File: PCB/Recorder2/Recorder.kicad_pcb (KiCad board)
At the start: 2 copper layers, 70 x 70 mm, 57 parts, among them J1 Reset, J2 JST-PH-SM4-TB, J3 TC2030-USB-NL-DS, J4 TF_PUSH, J5 USB-C-Socket-H, Q1 CJ2301, SW1 SW_Push_DPDT, U1 ESP32-S3-MINI-1-N4R2, U3 TP4054, U4 ME6211C33M5G-N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

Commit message: Tracked for order
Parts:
- moved R1 11.9 mm to (109.2, 108.4), turned to -90 degrees
- moved R14 11.5 mm to (93.0, 109.3), turned to 90 degrees
- moved R15 10.7 mm to (92.0, 109.3), turned to -90 degrees
- moved R16 9.90 mm to (91.0, 109.3), turned to 90 degrees
- moved J1 2.30 mm to (120.2, 105.7)
- moved C2 1.98 mm to (108.4, 92.7)
- moved R8 1.52 mm to (111.6, 92.9), turned to 0 degrees
- moved C15 1.50 mm to (89.0, 92.0)
- moved R2 1.32 mm to (109.0, 92.1)
- moved D9 1.00 mm to (90.5, 92.0)
- moved C14 0.70 mm to (106.2, 110.3)
- moved C13 0.42 mm to (89.0, 107.0)
- turned J3 to 0 degrees
- turned R12 to 180 degrees
- turned R13 to 0 degrees
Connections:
- net VIN renamed Net-(D3-K)
- R1 pad 1: Net-(U1-GPIO41) -> Net-(U1-GPIO48)
- U1 pad 12: LEDMIC -> unconnected-(U1-GPIO8-Pad12)
- U1 pad 13: unconnected-(U1-GPIO9-Pad13) -> LEDMIC
- U1 pad 14: unconnected-(U1-GPIO10-Pad14) -> ADC
- U1 pad 15: CHARGING -> ADCL
- U1 pad 29: unconnected-(U1-GPIO34-Pad29) -> BLINK
- U1 pad 30: unconnected-(U1-GPIO48-Pad30) -> Net-(U1-GPIO48)
- U1 pad 35: BLINK -> unconnected-(U1-GPIO39-Pad35)
- U1 pad 37: Net-(U1-GPIO41) -> unconnected-(U1-GPIO41-Pad37)
- U1 pad 5: BTN -> CHARGING
- U1 pad 7: unconnected-(U1-GPIO3-Pad7) -> BTN
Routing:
- net +3V3: track 0.00 -> 113.6 mm, vias 0 -> 7
- net GND: track 0.00 -> 75.2 mm, vias 0 -> 30
- net VSWITCHED: track 0.00 -> 61.8 mm, vias 0 -> 3
- net D-: track 0.00 -> 55.7 mm, vias 0 -> 2
- net D+: track 0.00 -> 55.1 mm, vias 0 -> 2
- net VBUS: track 0.00 -> 33.3 mm, vias 0 -> 2
- net SCK: track 0.00 -> 32.5 mm, vias 0 -> 3
- net WS: track 0.00 -> 31.0 mm, vias 0 -> 4
- net PWR: track 0.00 -> 28.9 mm, vias 0 -> 2
- net VBAT: track 0.00 -> 25.9 mm, vias 0 -> 2
- net SD: track 0.00 -> 25.6 mm, vias 0 -> 1
- net BTN: track 0.00 -> 23.6 mm, vias 0 -> 2
- net Net-(J1-Pin_2): track 0.00 -> 23.1 mm, vias 0 -> 3
- net CHARGING: track 0.00 -> 18.4 mm, vias 0 -> 2
- net Net-(D7-O): track 0.00 -> 18.1 mm, vias 0 -> 2
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- added copper zone on F.Cu, net VBUS
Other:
- board text added: "${CURRENT_DATE}"
- board text added: "1 2 3 5 6 7 9 10 11"
- board text added: "12 13 14 15 16 17 18"
- board text added: "34 48"
- board text added: "A"
- board text added: "Baking not required X-ray not required"
- board text added: "CHG PWR BTN SCK WS SD LEDMIC ADC ADCL"
- board text added: "DAT2 DAT3 CMD CLK DAT0 DAT1 CD"
- board text added: "L"
- board text added: "LEDS VBUS"
- board text added: "Made in China for Andrews&Arnold Ltd"
- board text added: "OpenMic"
- board text added: "R"
- board text added: "openmic.revk.uk"
- board text removed: "Baking not required"

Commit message: Re render
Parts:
- C10, C11: footprint RevK:C_0402 -> RevK:C_0201
- R11, R14, R15, R16: footprint RevK:R_0402 -> RevK:R_0201
- R8: value 10K -> 5K1; footprint RevK:R_0402 -> RevK:R_0201
- U5: value L -> ICS-43434
- U6: value R -> ICS-43434
- moved U5 21.0 mm to (87.0, 89.0), turned to 90 degrees
- moved U6 21.0 mm to (87.0, 110.0), turned to -90 degrees
- moved D1 0.80 mm to (118.2, 100.0)
- moved J5 0.50 mm to (119.5, 92.5)
- moved D2 0.40 mm to (120.1, 100.5)
- moved R14 0.32 mm to (92.7, 109.2), turned to -90 degrees
- moved R16 0.32 mm to (91.3, 109.2), turned to -90 degrees
- moved J4 0.10 mm to (94.7, 100.5)
- moved R15 0.10 mm to (92.0, 109.2), turned to 90 degrees
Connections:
- R16 pad 2: ADCL -> GND
- U1 pad 14: ADC -> unconnected-(U1-GPIO10-Pad14)
- U1 pad 15: ADCL -> ADC
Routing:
- net ADC: track 12.4 -> 4.28 mm, vias 2 -> 0
- net ADCL: track 3.91 -> 0.00 mm
- net +3V3: track 113.6 -> 109.9 mm
- net VBAT: track 25.9 -> 28.2 mm
- net GND: track 75.2 -> 74.2 mm, vias 30 -> 33
- net VSWITCHED: track 61.8 -> 62.7 mm
- net PWR: track 28.9 -> 28.2 mm
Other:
- board text added: "1 2 3 5 6 7 9 11"
- board text added: "Audio Recorder"
- board text added: "CHG PWR BTN SCK WS SD LEDMIC ADC"
- board text removed: "1 2 3 5 6 7 9 10 11"
- board text removed: "CHG PWR BTN SCK WS SD LEDMIC ADC ADCL"

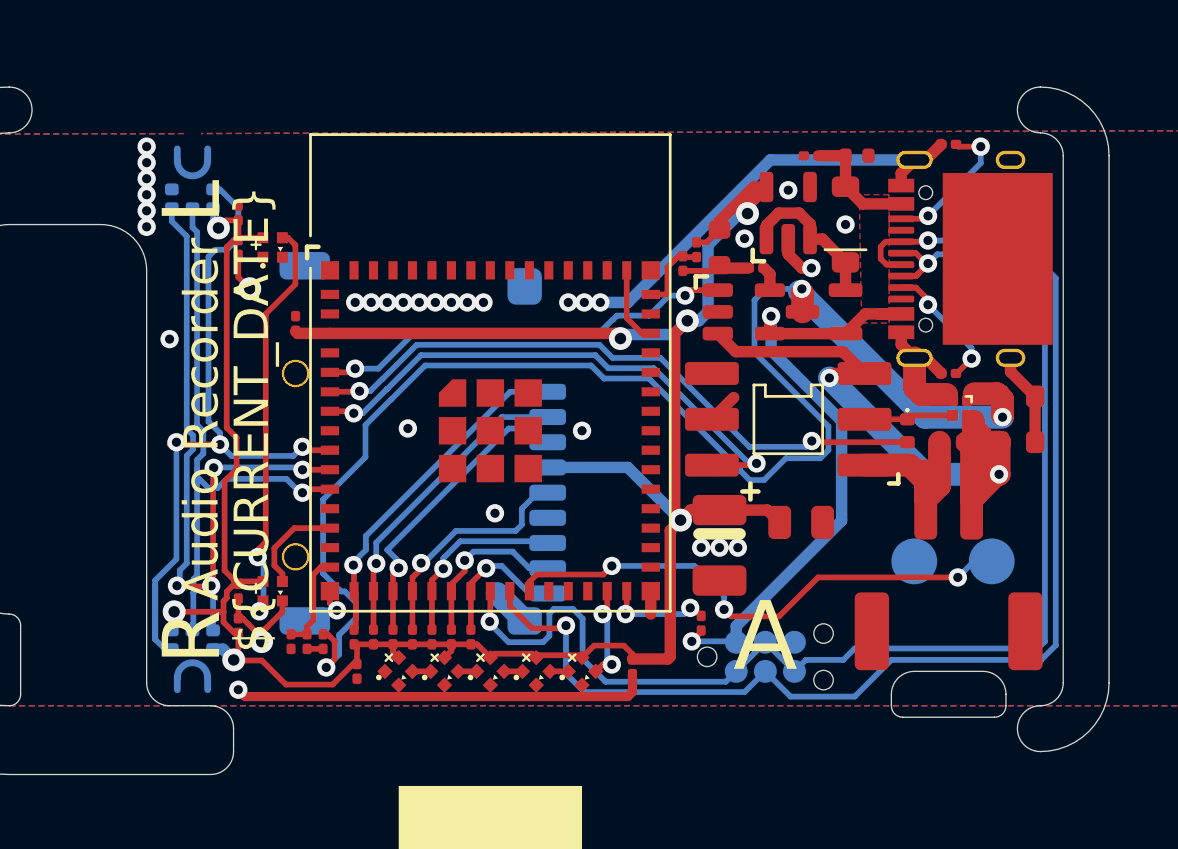
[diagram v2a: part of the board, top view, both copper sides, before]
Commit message: Layout tweaks
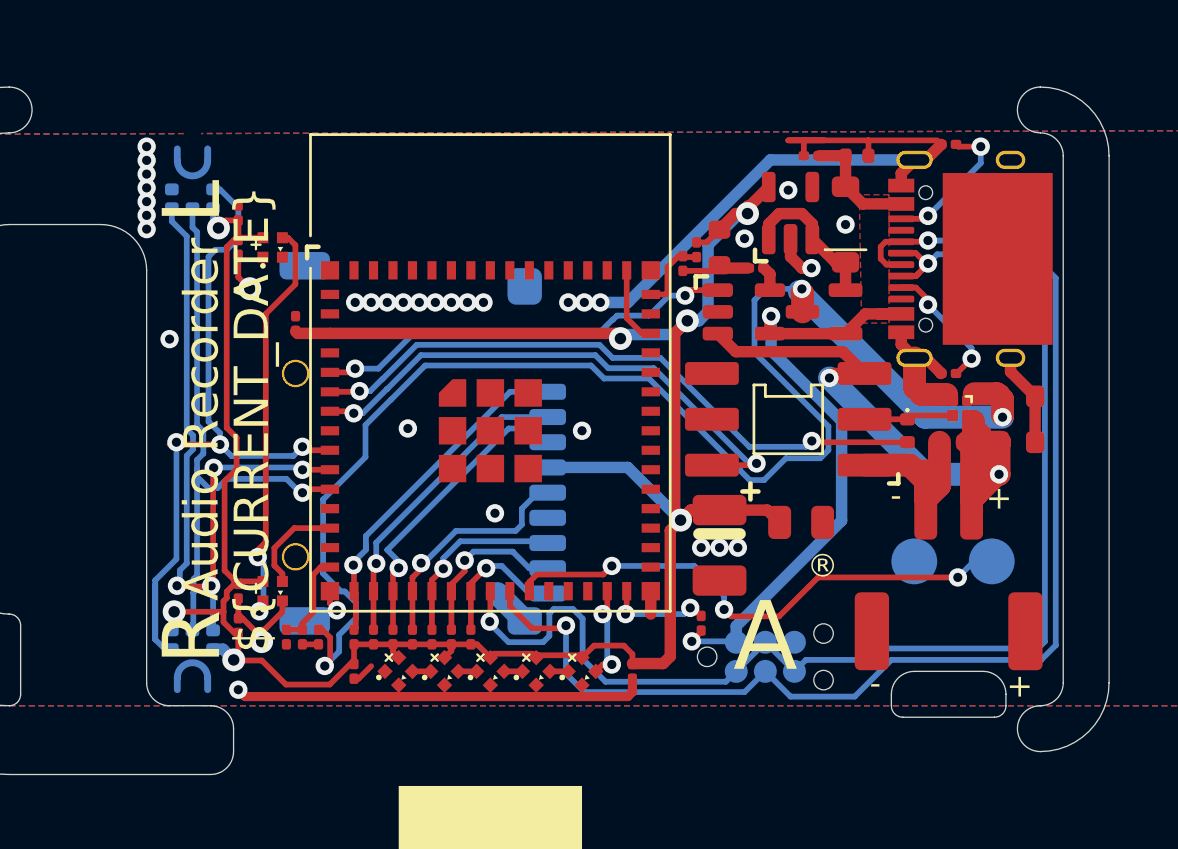
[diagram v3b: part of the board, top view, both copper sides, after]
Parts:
- U2: value ~ -> TPS22916CNYFPR
- moved R14 0.28 mm to (92.5, 109.0)
- moved R15 0.28 mm to (91.8, 109.0)
- moved R16 0.28 mm to (91.1, 109.0)
- moved C14 0.20 mm to (106.2, 110.5)
- moved C12 0.13 mm to (94.0, 110.5)
- moved U4 0.10 mm to (113.1, 90.5)
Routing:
- net GND: track 74.2 -> 83.0 mm, vias 33 -> 34
- net +3V3: track 109.9 -> 108.7 mm
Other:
- board text added: "+"
- board text added: "-"
- board text added: "21"
- board text added: "®"

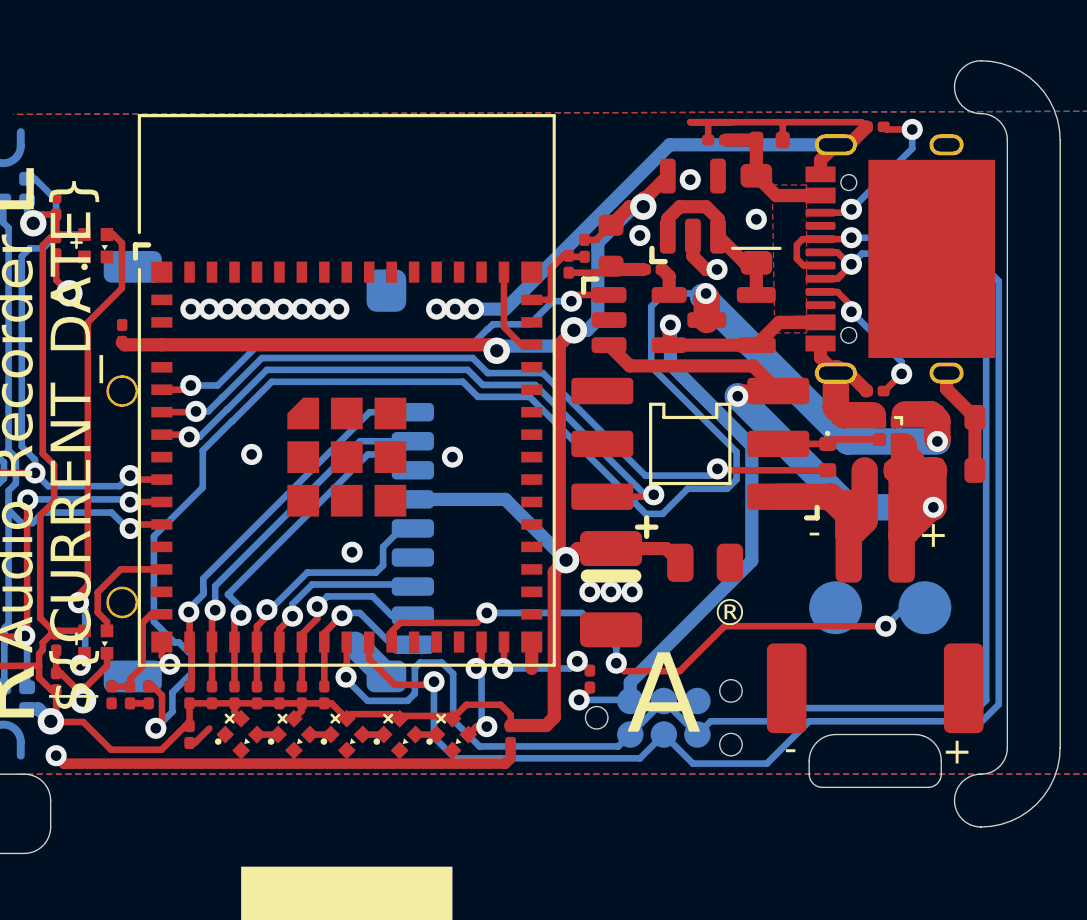
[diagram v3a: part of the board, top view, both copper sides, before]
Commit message: Moved GPIOs around a bit
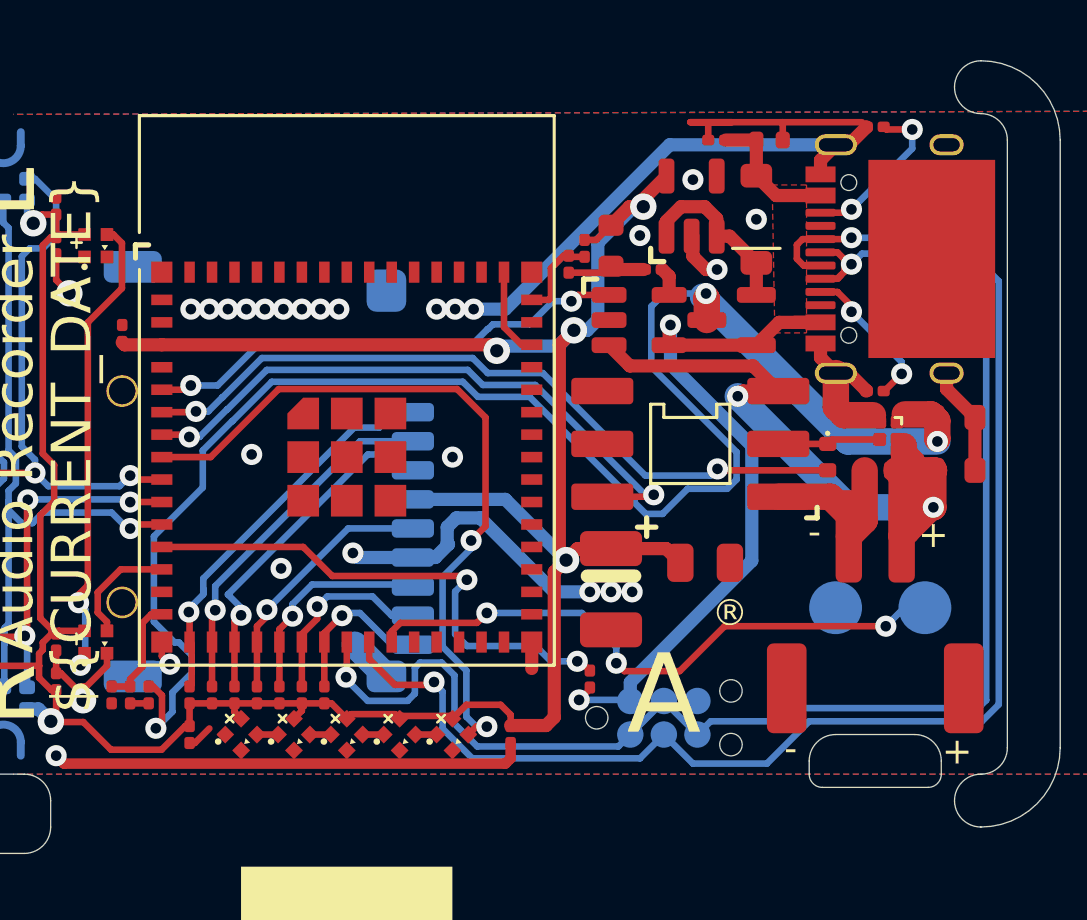
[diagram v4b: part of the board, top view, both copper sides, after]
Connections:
- R1 pad 1: Net-(U1-GPIO48) -> Net-(U1-GPIO8)
- U1 pad 12: unconnected-(U1-GPIO8-Pad12) -> Net-(U1-GPIO8)
- U1 pad 29: BLINK -> unconnected-(U1-GPIO34-Pad29)
- U1 pad 30: Net-(U1-GPIO48) -> unconnected-(U1-GPIO48-Pad30)
- U1 pad 8: unconnected-(U1-GPIO4-Pad8) -> BLINK
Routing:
- net BLINK: track 4.27 -> 27.9 mm
- net Net-(U1-GPIO8): track 0.00 -> 20.0 mm, vias 0 -> 2
- net GND: track 83.0 -> 92.1 mm, vias 34 -> 35
- net Net-(U1-GPIO48): track 4.58 -> 0.00 mm, vias 2 -> 0
- net Net-(J1-Pin_2): track 23.1 -> 22.3 mm
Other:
- board text added: "4 8"
- board text removed: "34 48"

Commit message: Tidy
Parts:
- removed J2: JST-PH-SM4-TB, RevK:JST_PH_S2B-PH-SM4-TB_1x02-1MP_P2.00mm_Horizontal
- added J6: Battery, RevK:1.25T-2PWT (Molex 532610271), F.Cu at (120.2, 107.0)
- moved U5 0.50 mm to (87.5, 89.0)
- moved U6 0.50 mm to (87.5, 110.0)
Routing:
- net GND: track 92.1 -> 86.4 mm, vias 35 -> 36
- net WS: track 31.0 -> 25.7 mm
- net SCK: track 32.5 -> 29.5 mm
- net VBAT: track 28.2 -> 31.1 mm
- net Net-(J1-Pin_2): track 22.3 -> 24.4 mm

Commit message: Twqeak
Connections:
- SW1 pad 1: GND -> unconnected-(SW1-A-Pad1)

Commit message: beep bug
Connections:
- net VBAT renamed VBATCHG
